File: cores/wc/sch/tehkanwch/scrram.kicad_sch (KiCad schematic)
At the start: 22 parts

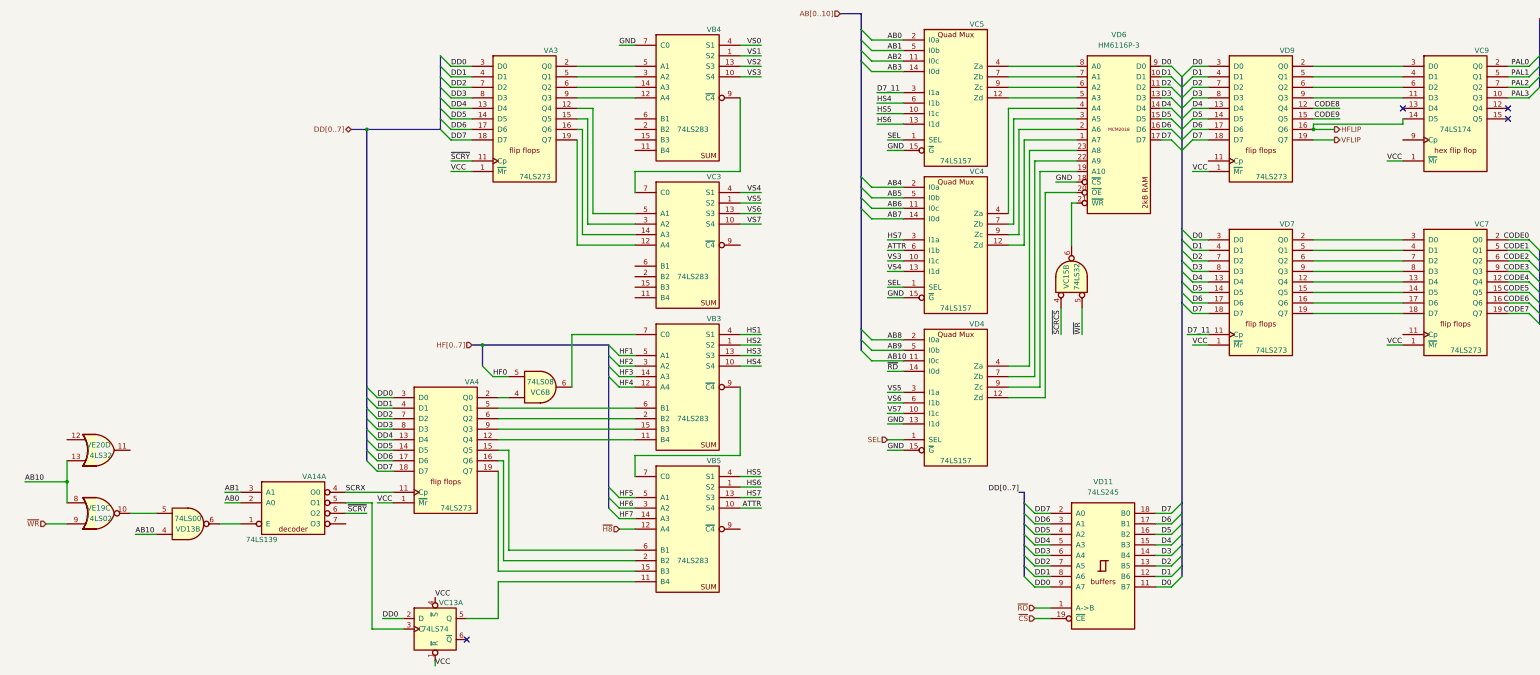
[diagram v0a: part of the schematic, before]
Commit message: wc: all modules connected
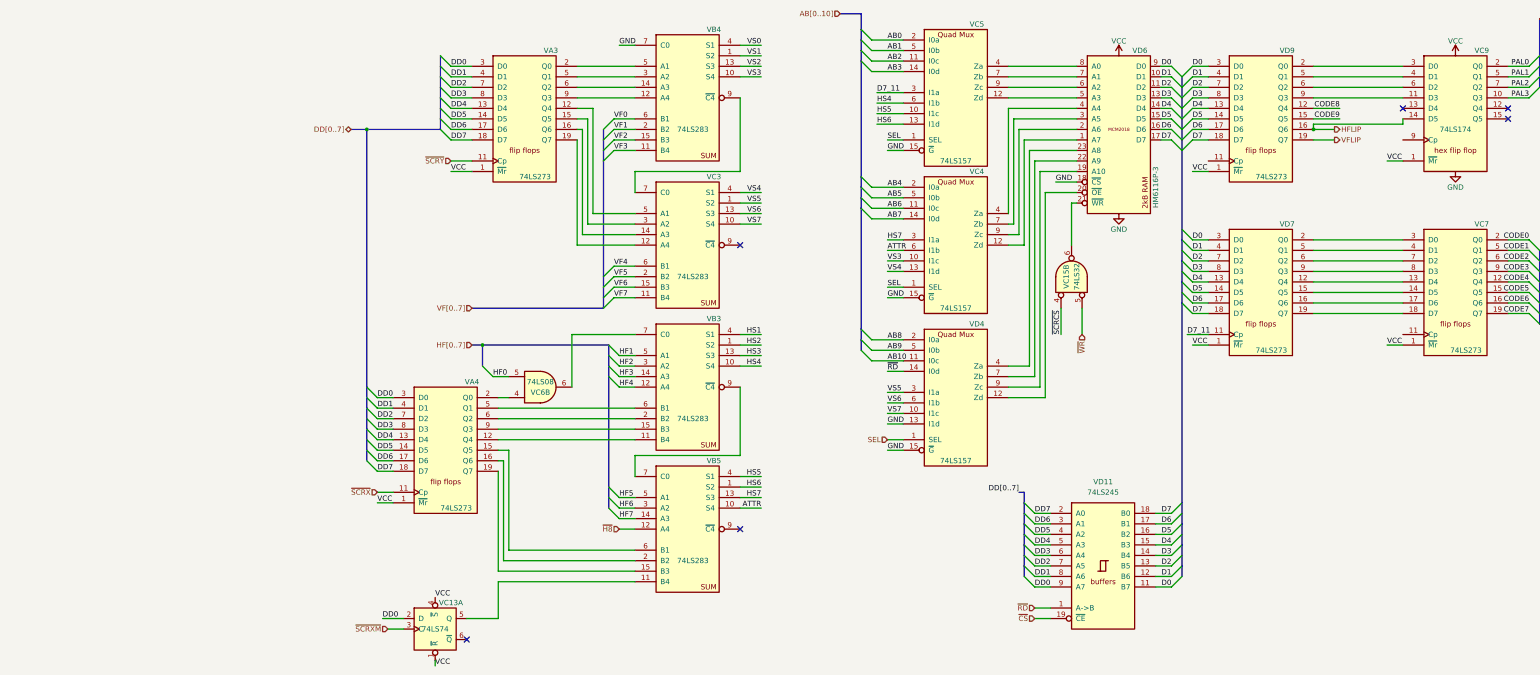
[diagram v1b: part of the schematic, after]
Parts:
- removed VA14: 74LS139, symbol jt74:74LS139
- removed VD13: 74LS00, symbol jt74:74LS00
- removed VE19: 74LS02, symbol jt74:74LS02
- removed VE20: 74LS32, symbol jt74:74LS32
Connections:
- net VSS is gone; now on net GND: VC9.8 (VSS), VD6.12 (VSS)
- net VF7: now reaches VC3.11 (B4)
- net VF6: now reaches VC3.15 (B3)
- net VF5: now reaches VC3.2 (B2)
- net VF4: now reaches VC3.6 (B1)
- net ~{SCRXM}: now reaches VC13.3 (C)
- net VF3: now reaches VB4.11 (B4)
- net VF2: now reaches VB4.15 (B3)
- net VF1: now reaches VB4.2 (B2)
- net VF0: now reaches VB4.6 (B1)
- net SCRX renamed ~{SCRX}
- no-connect marks 4 -> 6

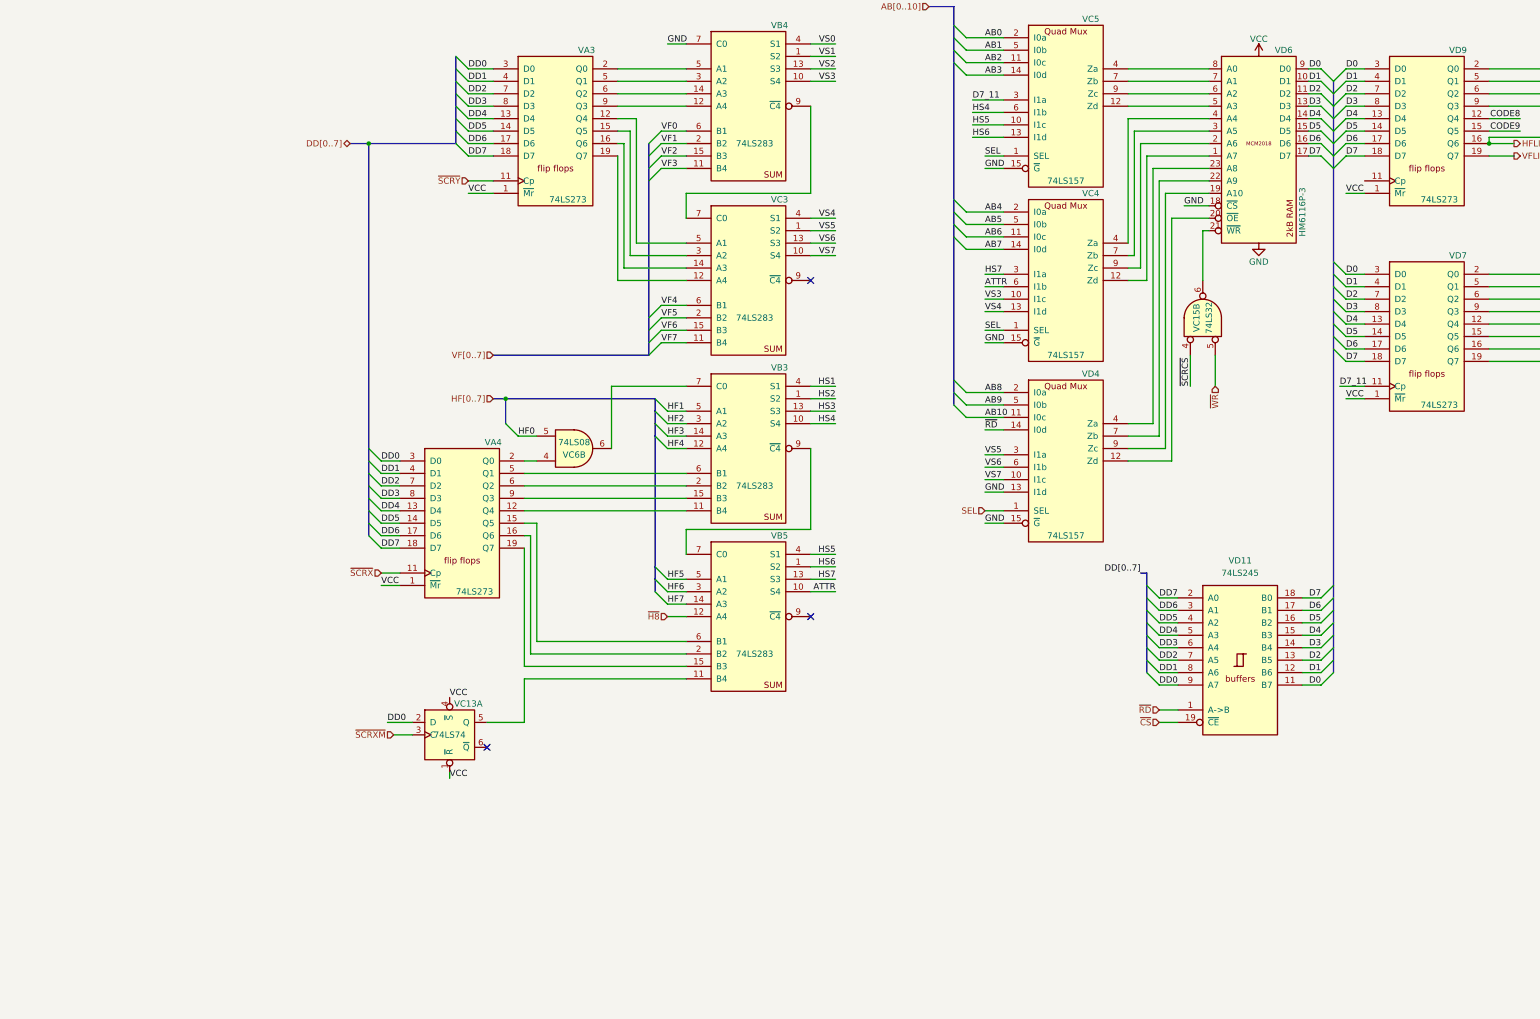
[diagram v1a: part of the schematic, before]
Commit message: wc: tehkanwch shows the grid screen but then halts
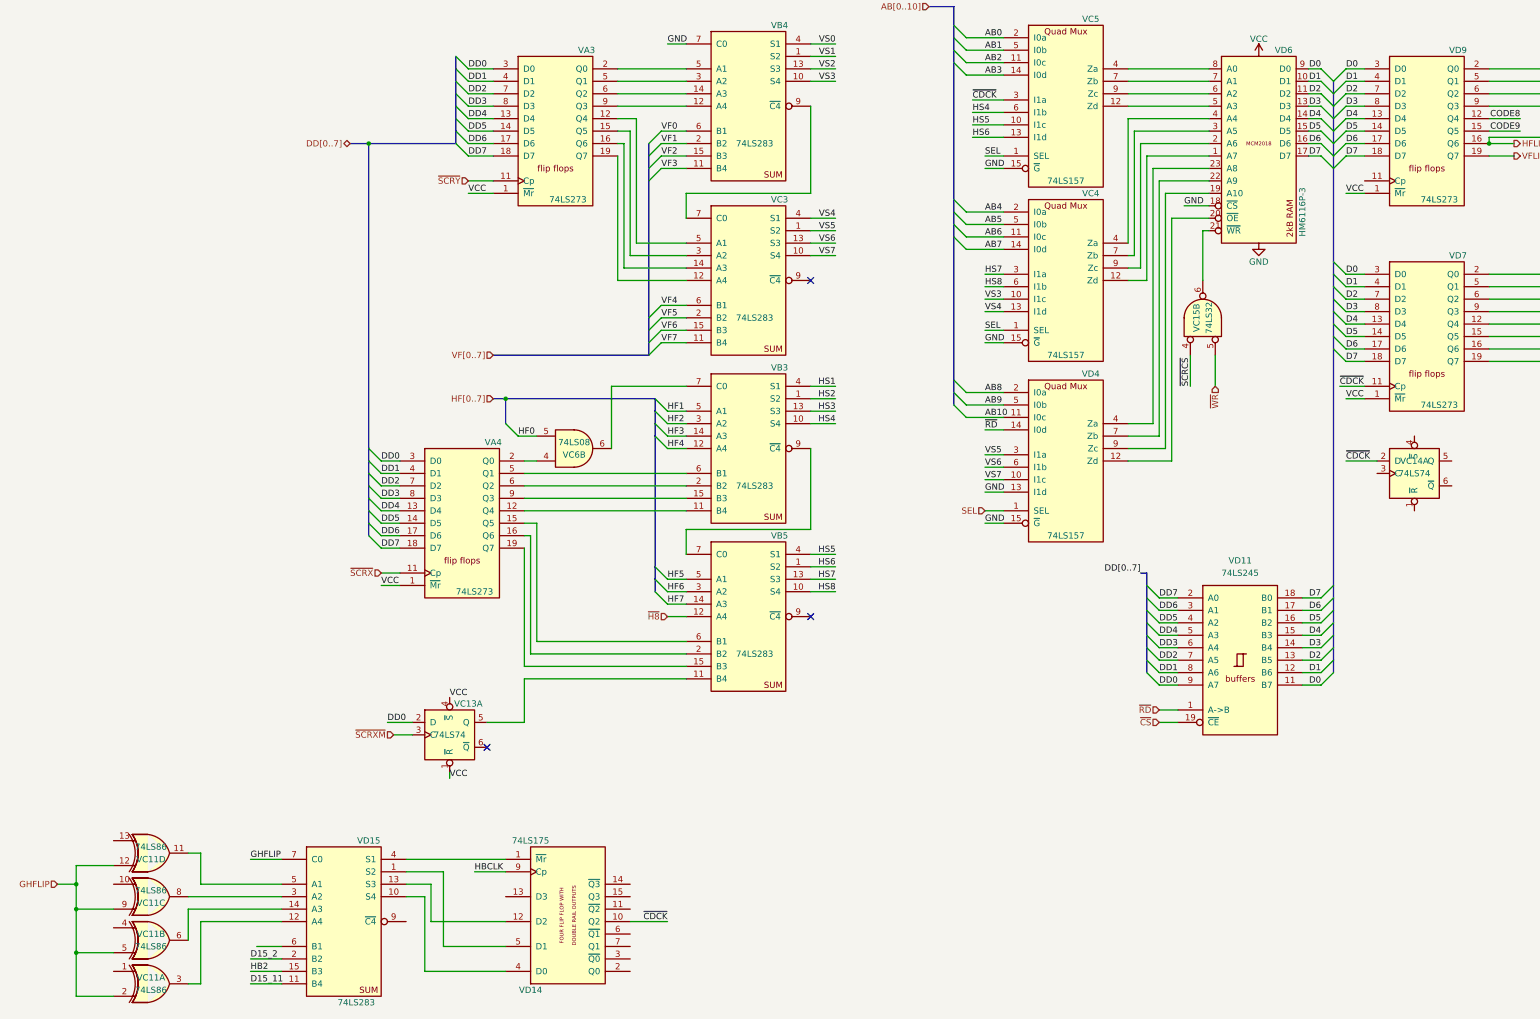
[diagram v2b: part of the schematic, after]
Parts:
- added VC11: 74LS86, symbol jt74:74LS86
- added VC14: 74LS74, symbol jt74:74LS74
- added VD14: 74LS175, symbol jt74:74LS175
- added VD15: 74LS283, symbol jt74:74LS283
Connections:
- net ATTR renamed HS8
- net D7_11 renamed ~{CDCK}
- net ~{CDCK}: now also VC14.2 (D), VD14.10 (Q2)
- new net: VC11.11, VD15.5 (A1)
- new net: VC11.8, VD15.3 (A2)
- new net: VD14.1 (~{Mr}), VD15.4 (S1)
- new net: VD14.12 (D2), VD15.13 (S3)
- new net: VD14.4 (D0), VD15.10 (S4)
- new net: VD14.5 (D1), VD15.1 (S2)
- new net: VC11.6, VD15.14 (A3)
- new net: VC11.3, VD15.12 (A4)
- new net D15_11: VD15.11 (B4)
- new net D15_2: VD15.2 (B2)
- new net GHFLIP: VC11.12, VC11.2, VC11.5, VC11.9, VD15.7 (C0)
- new net HB2: VD15.15 (B3)
- new net HBCLK: VD14.9 (Cp)

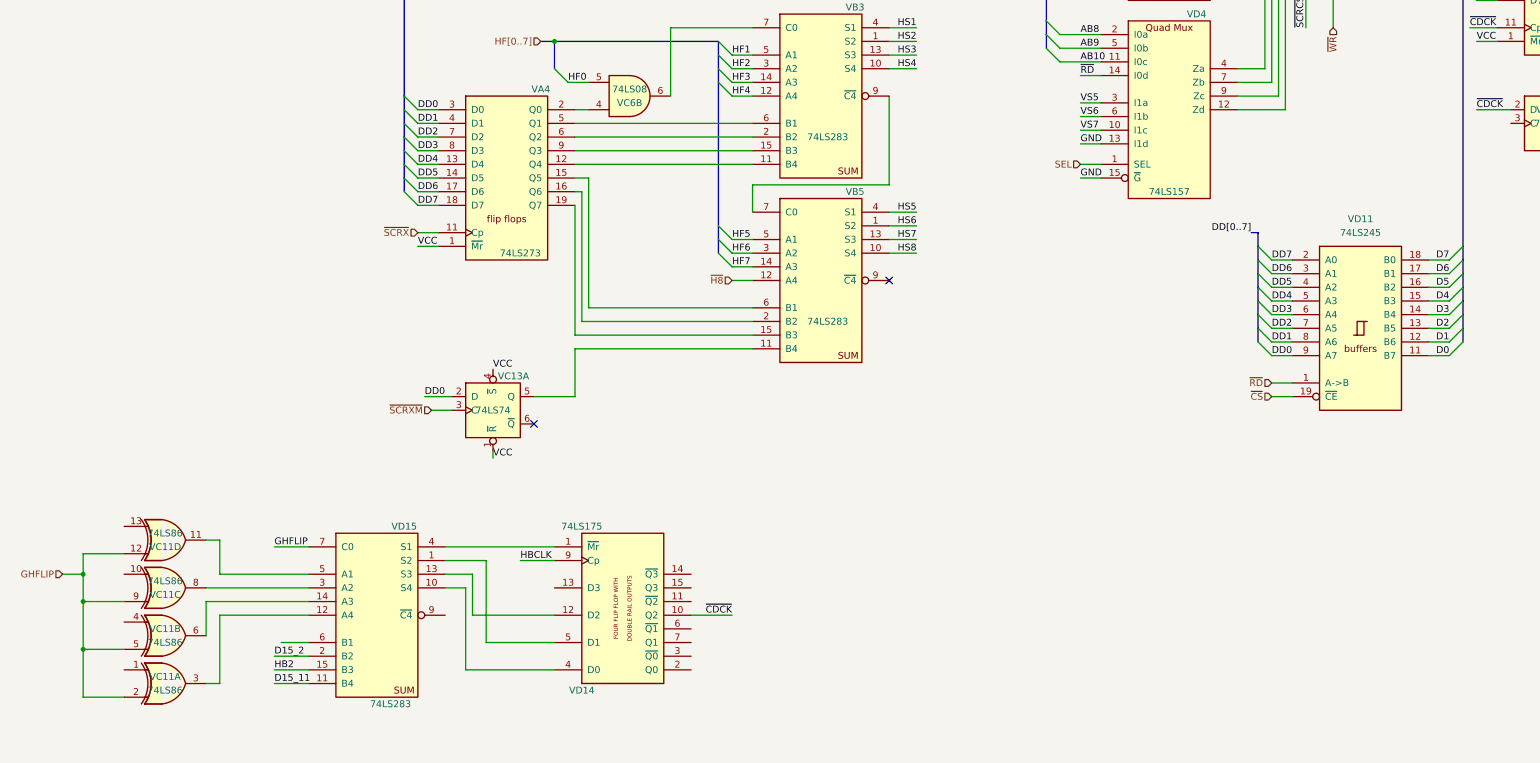
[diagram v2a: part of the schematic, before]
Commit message: wc sch: sub CPU address bus connection to shared memory
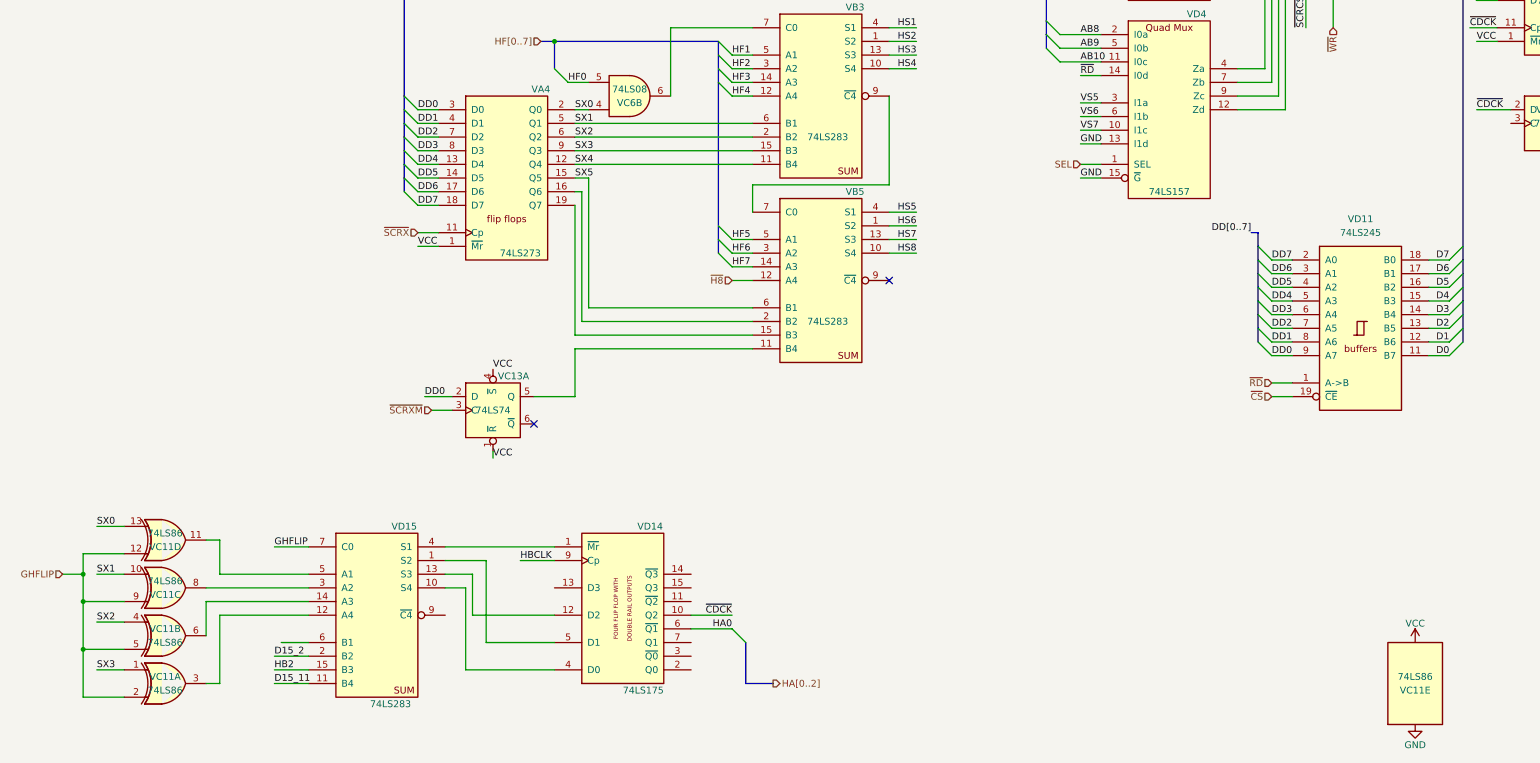
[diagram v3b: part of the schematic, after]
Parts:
- added unit 5 of VC11
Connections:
- net VCC is gone; now on net GND: VA3.1 (~{Mr}), VA4.1 (~{Mr}), VC13.1 (~{R}), VC13.4 (~{S}), VC7.1 (~{Mr}), VC9.1 (~{Mr}), VC9.16 (VCC), VD6.24 (VCC), VD7.1 (~{Mr}), VD9.1 (~{Mr})
- net GND: now also VC11.14 (VCC), VC11.7 (VSS)
- net SX0: now reaches VC11.13
- net SX0: now also VA4.2 (Q0), VC6.4
- net SX1: now reaches VC11.10
- net SX1: now also VA4.5 (Q1), VB3.6 (B1)
- net SX4: now reaches VA4.12 (Q4), VB3.11 (B4)
- net SX5: now reaches VA4.15 (Q5), VB5.6 (B1)
- net SX2: now reaches VA4.6 (Q2), VB3.2 (B2)
- net SX2: now also VC11.4
- net SX3: now reaches VA4.9 (Q3), VB3.15 (B3)
- net SX3: now also VC11.1
- net HA0: now reaches VD14.6 (~{Q1})

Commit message: wc: obj module -wip-
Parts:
- added unit 2 of VC14
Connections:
- net ~{SCRCS} is gone; now on net ~{CS}: VC15.4
- net GND: now also VC14.1 (~{R}), VC14.4 (~{S}), VC14.10 (~{S}), VC14.13 (~{R})
- net ATCK: now reaches VD9.11 (Cp)
- net ATCK: now also VC7.11 (Cp), VC14.8 (~{Q})
- net HA2*: now reaches VD14.15 (Q3)
- net HA2*: now also VC9.9 (Cp), VC14.12 (D)
- net HA1*: now reaches VD14.7 (Q1)
- net HA1*: now also VC14.3 (C)
- net at VC14.5 (Q): now also VC14.11 (C)
- net HA1: now reaches VC14.6 (~{Q})
- new net HA2: VC14.9 (Q)
- no-connect marks 6 -> 7
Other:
- moved on the sheet: VC13A, VC14A

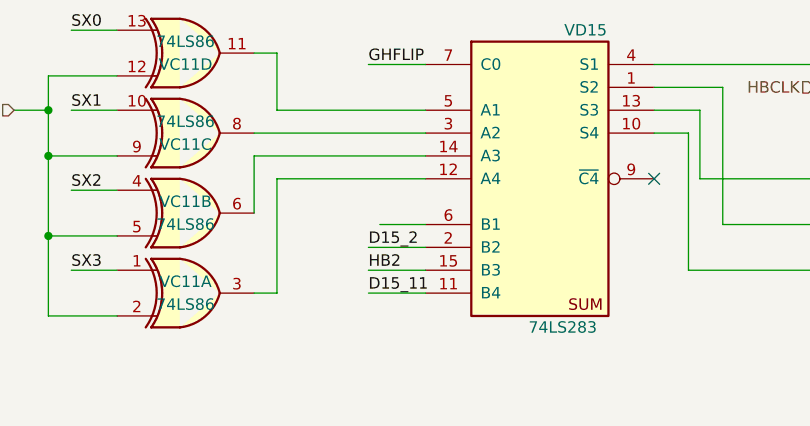
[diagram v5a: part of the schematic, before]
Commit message: wc: playable using tehkanwch controls
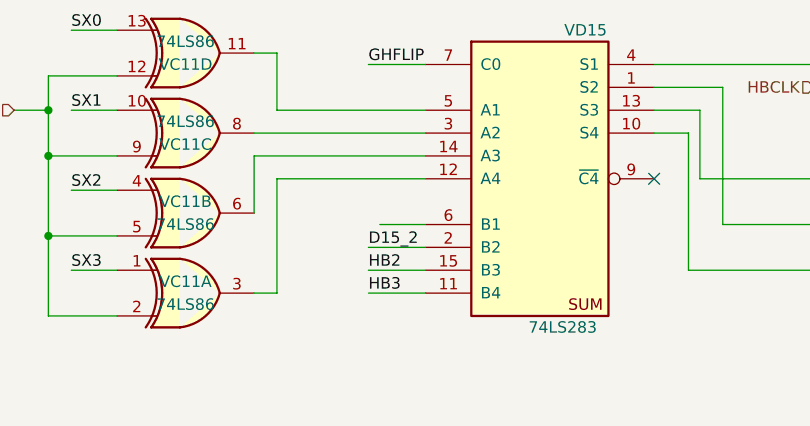
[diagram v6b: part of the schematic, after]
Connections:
- net D15_11 renamed HB3
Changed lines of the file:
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@@
 		)
 	)
-	(label "D15_11"
+	(label "HB3"
 		(at 74.93 262.89 0)
 		(fields_autoplaced yes)
